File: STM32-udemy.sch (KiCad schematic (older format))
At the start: 20 parts

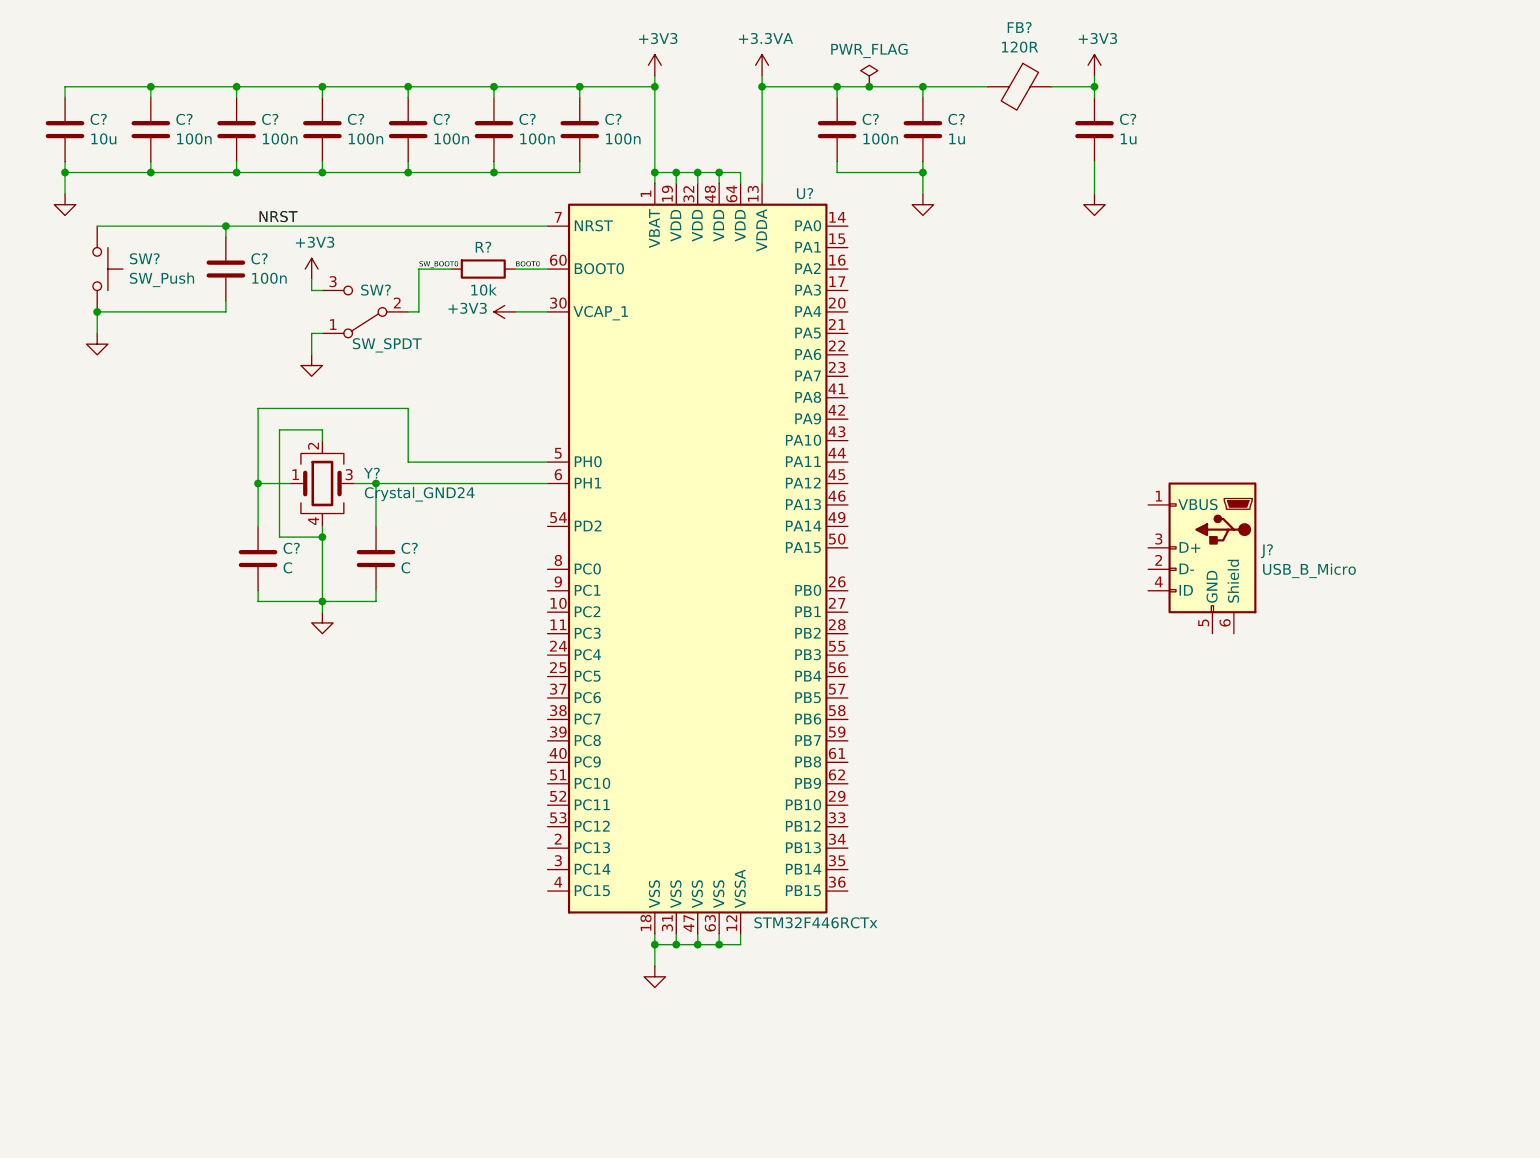
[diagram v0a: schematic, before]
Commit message: Add USB and Serial Wire schematic
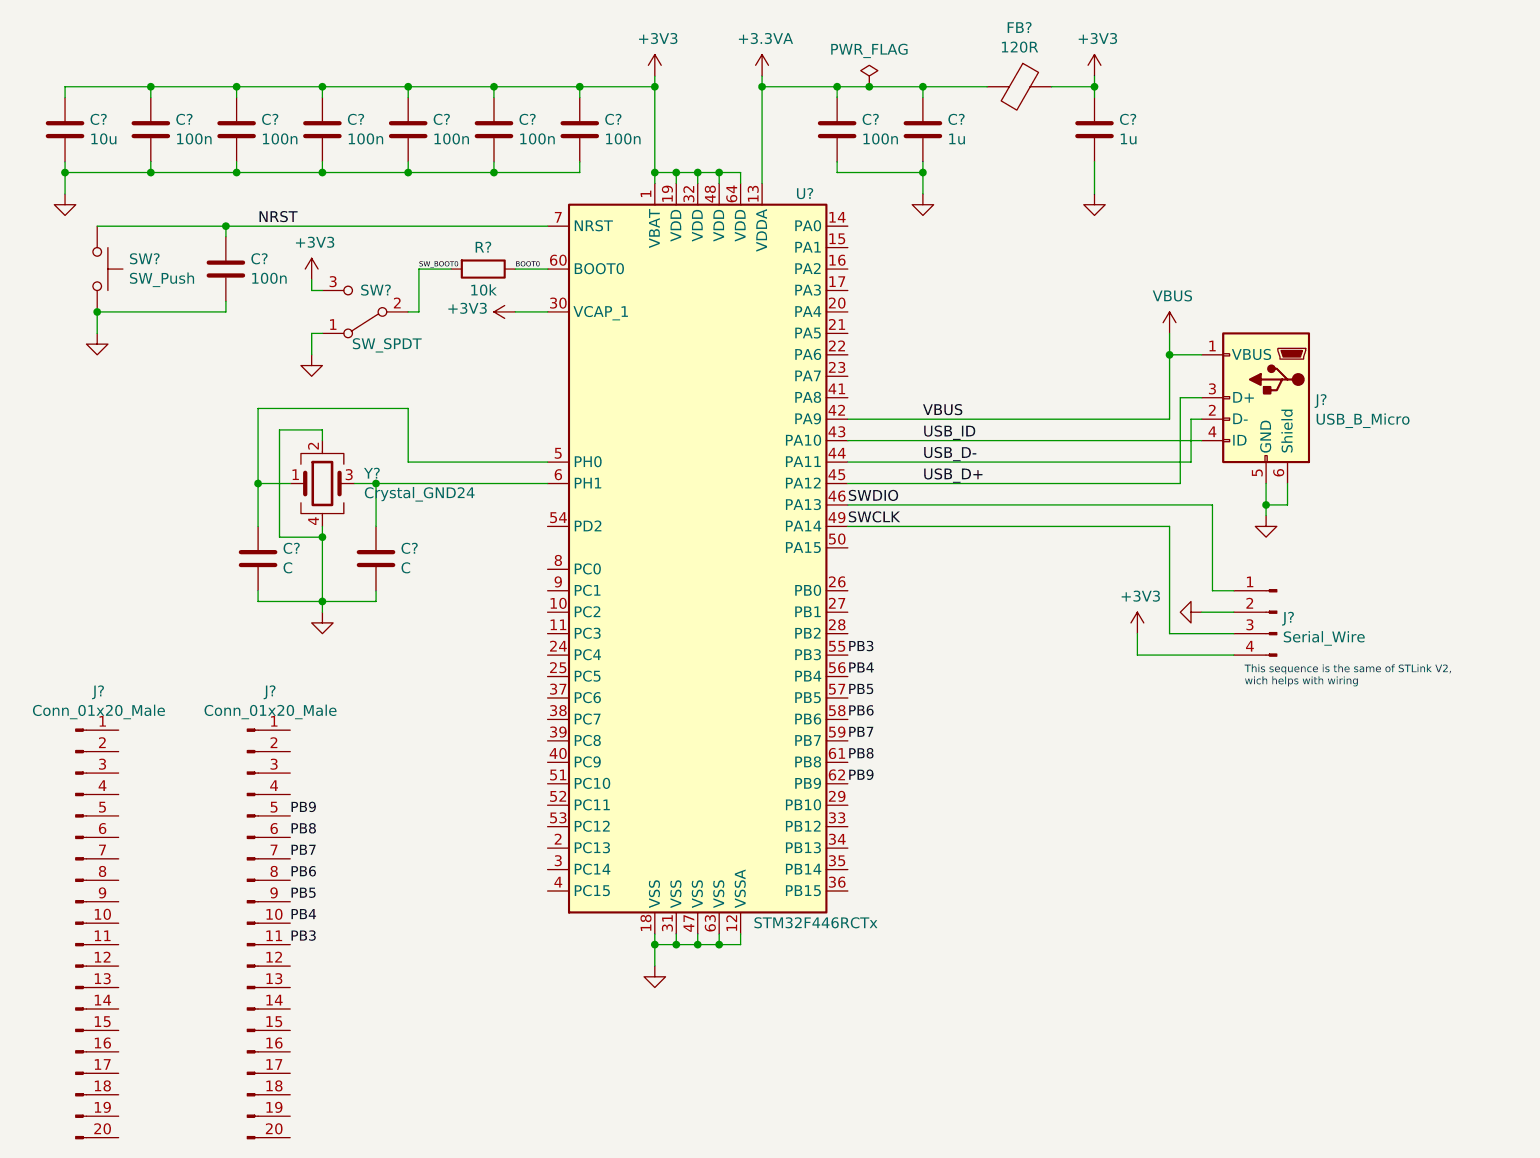
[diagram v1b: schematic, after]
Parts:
- added J?: Serial_Wire, symbol Connector:Conn_01x04_Male
- added J? (x2): Conn_01x20_Male, symbol Connector:Conn_01x20_Male
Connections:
- net +3V3: now also J?.4 (Pin_4)
- net GND: now also J?.5 (GND), J?.6 (Shield), J?.2 (Pin_2)
- net VBUS: now reaches U?.42 (PA9)
- net VBUS: now also J?.1 (VBUS)
- net USB_ID: now reaches U?.43 (PA10)
- net USB_ID: now also J?.4 (ID)
- net USB_D-: now reaches U?.44 (PA11)
- net USB_D-: now also J?.2 (D-)
- net USB_D+: now reaches U?.45 (PA12)
- net USB_D+: now also J?.3 (D+)
- net SWDIO: now reaches U?.46 (PA13)
- net SWDIO: now also J?.1 (Pin_1)
- net SWCLK: now reaches U?.49 (PA14)
- net SWCLK: now also J?.3 (Pin_3)
- net PB3: now reaches U?.55 (PB3)
- net PB3: now also J?.11 (Pin_11)
- net PB4: now reaches U?.56 (PB4)
- net PB4: now also J?.10 (Pin_10)
- net PB5: now reaches U?.57 (PB5)
- net PB5: now also J?.9 (Pin_9)
- net PB6: now reaches U?.58 (PB6)
- net PB6: now also J?.8 (Pin_8)
- net PB7: now reaches U?.59 (PB7)
- net PB7: now also J?.7 (Pin_7)
- net PB8: now reaches U?.61 (PB8)
- net PB8: now also J?.6 (Pin_6)
- net PB9: now reaches U?.62 (PB9)
- net PB9: now also J?.5 (Pin_5)
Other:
- note added: "This sequence is the same of STLink V2,\nwich helps with wiring"
- moved on the sheet: J?
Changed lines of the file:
@@
 Wire Wire Line
 	3950 3250 3850 3250
+Text Label 6500 3150 0    50   ~ 0
+USB_D-
+Text Label 6500 3250 0    50   ~ 0
+USB_D+
+Text Label 6150 3350 0    50   ~ 0
+SWDIO
+Text Label 6150 3450 0    50   ~ 0
+SWCLK
+Text Label 6500 2950 0    50   ~ 0
+VBUS
+Text Label 6500 3050 0    50   ~ 0
+USB_ID
 $Comp
 L Connector:USB_B_Micro J?
 U 1 1 62056208
-P 7850 3550
-F 0 "J?" H 7620 3539 50  0000 R CNN
-F 1 "USB_B_Micro" H 7620 3448 50  0000 R CNN
-F 2 "" H 8000 3500 50  0001 C CNN
-F 3 "~" H 8000 3500 50  0001 C CNN
-	1    7850 3550
+P 8100 2850
+F 0 "J?" H 7870 2839 50  0000 R CNN
+F 1 "USB_B_Micro" H 7870 2748 50  0000 R CNN
+F 2 "" H 8250 2800 50  0001 C CNN
+F 3 "~" H 8250 2800 50  0001 C CNN
+	1    8100 2850
 	-1   0    0    -1
 $EndComp
+Wire Wire Line
+	6150 3050 7800 3050
+Wire Wire Line
+	6150 3150 7750 3150
+Wire Wire Line
+	7750 3150 7750 2950
+Wire Wire Line
+	7750 2950 7800 2950
+Wire Wire Line
+	7700 3250 7700 2850
+Wire Wire Line
+	7700 2850 7800 2850
+Wire Wire Line
+	6150 3250 7700 3250
+Wire Wire Line
+	7650 2950 7650 2650
+Wire Wire Line
+	7650 2650 7800 2650
+Wire Wire Line
+	6150 2950 7650 2950
+$Comp
+L power:VBUS #PWR?
+U 1 1 620605D0
+P 7650 2550
+F 0 "#PWR?" H 7650 2400 50  0001 C CNN
+F 1 "VBUS" H 7665 2723 50  0000 C CNN
+F 2 "" H 7650 2550 50  0001 C CNN
+F 3 "" H 7650 2550 50  0001 C CNN
+	1    7650 2550
+	1    0    0    -1
+$EndComp
+Wire Wire Line
+	7650 2550 7650 2650
+Connection ~ 7650 2650
+$Comp
+L power:GND #PWR?
+U 1 1 62064E84
+P 8100 3400
+F 0 "#PWR?" H 8100 3150 50  0001 C CNN
+F 1 "GND" H 8105 3227 50  0001 C CNN
+F 2 "" H 8100 3400 50  0001 C CNN
+F 3 "" H 8100 3400 50  0001 C CNN
+	1    8100 3400
+	1    0    0    -1
+$EndComp
+Wire Wire Line
+	8100 3400 8100 3350
+Wire Wire Line
+	8200 3250 8200 3350
+Wire Wire Line
+	8200 3350 8100 3350
+Connection ~ 8100 3350
+Wire Wire Line
+	8100 3350 8100 3250
+$Comp
+L Connector:Conn_01x04_Male J?
+U 1 1 6206CBAD
+P 8150 3850
+F 0 "J?" H 8122 3824 50  0000 R CNN
+F 1 "Serial_Wire" H 8122 3733 50  0000 R CNN
+F 2 "" H 8150 3850 50  0001 C CNN
+F 3 "~" H 8150 3850 50  0001 C CNN
+	1    8150 3850
+	-1   0    0    -1
+$EndComp
+Wire Wire Line
+	6150 3350 7850 3350
+Wire Wire Line
+	7850 3350 7850 3750
+Wire Wire Line
+	7850 3750 7950 3750
+Wire Wire Line
+	6150 3450 7650 3450
+Wire Wire Line
+	7650 3450 7650 3950
+Wire Wire Line
+	7650 3950 7950 3950
+$Comp
+L power:+3V3 #PWR?
+U 1 1 6207715A
+P 7500 3950
+F 0 "#PWR?" H 7500 3800 50  0001 C CNN
+F 1 "+3V3" H 7515 4123 50  0000 C CNN
+F 2 "" H 7500 3950 50  0001 C CNN
+F 3 "" H 7500 3950 50  0001 C CNN
+	1    7500 3950
+	1    0    0    -1
+$EndComp
+Wire Wire Line
+	7950 4050 7500 4050
+Wire Wire Line
+	7500 4050 7500 3950
+$Comp
+L power:GND #PWR?
+U 1 1 6208100C
+P 7800 3850
+F 0 "#PWR?" H 7800 3600 50  0001 C CNN
+F 1 "GND" H 7805 3677 50  0001 C CNN
+F 2 "" H 7800 3850 50  0001 C CNN
+F 3 "" H 7800 3850 50  0001 C CNN
+	1    7800 3850
+	0    1    1    0
+$EndComp
+Wire Wire Line
+	7800 3850 7950 3850
+Text Notes 8000 4200 0    35   ~ 0
+This sequence is the same of STLink V2,\nwich helps with wiring
+$Comp
+L Connector:Conn_01x20_Male J?
+U 1 1 62094D55
+P 2550 5300
+F 0 "J?" H 2658 6381 50  0000 C CNN
+F 1 "Conn_01x20_Male" H 2658 6290 50  0000 C CNN
+F 2 "" H 2550 5300 50  0001 C CNN
+F 3 "~" H 2550 5300 50  0001 C CNN
+	1    2550 5300
+	1    0    0    -1
+$EndComp
+$Comp
+L Connector:Conn_01x20_Male J?
+U 1 1 620964EC
+P 3350 5300
+F 0 "J?" H 3458 6381 50  0000 C CNN
+F 1 "Conn_01x20_Male" H 3458 6290 50  0000 C CNN
+F 2 "" H 3350 5300 50  0001 C CNN
+F 3 "~" H 3350 5300 50  0001 C CNN
+	1    3350 5300
+	1    0    0    -1
+$EndComp
+Text Label 6150 4050 0    47   ~ 0
+PB3
+Text Label 6150 4150 0    47   ~ 0
+PB4
+Text Label 6150 4250 0    47   ~ 0
+PB5
+Text Label 6150 4350 0    47   ~ 0
+PB6
+Text Label 6150 4450 0    47   ~ 0
+PB7
+Text Label 6150 4550 0    47   ~ 0
+PB8
+Text Label 6150 4650 0    47   ~ 0
+PB9
+Text Label 3550 5400 0    47   ~ 0
+PB3
+Text Label 3550 5300 0    47   ~ 0
+PB4
+Text Label 3550 5200 0    47   ~ 0
+PB5
+Text Label 3550 5100 0    47   ~ 0
+PB6
+Text Label 3550 5000 0    47   ~ 0
+PB7
+Text Label 3550 4900 0    47   ~ 0
+PB8
+Text Label 3550 4800 0    47   ~ 0
+PB9
 $EndSCHEMATC
